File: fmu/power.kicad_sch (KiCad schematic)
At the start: 49 parts, among them IC1 BQ7791500PWT, IC3 BQ25798RQMR, J1 1054500101, Q1 NDT3055L, Q2 NDT3055L, U9 MAX20075ATCA/V+

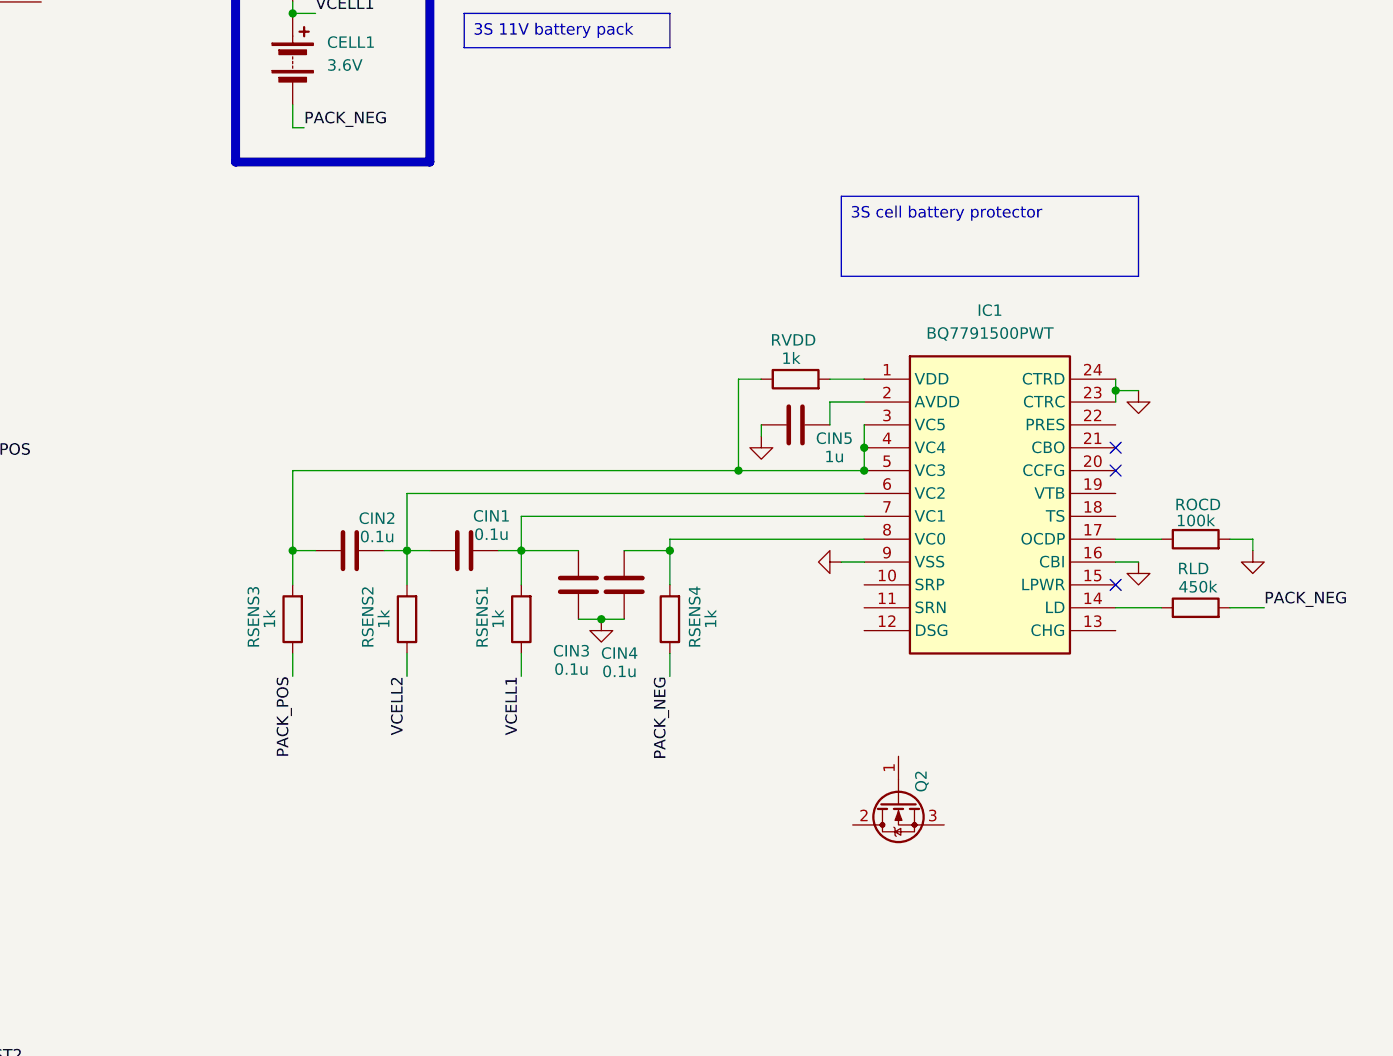
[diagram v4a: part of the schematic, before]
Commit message: BQ7791500 almost completed
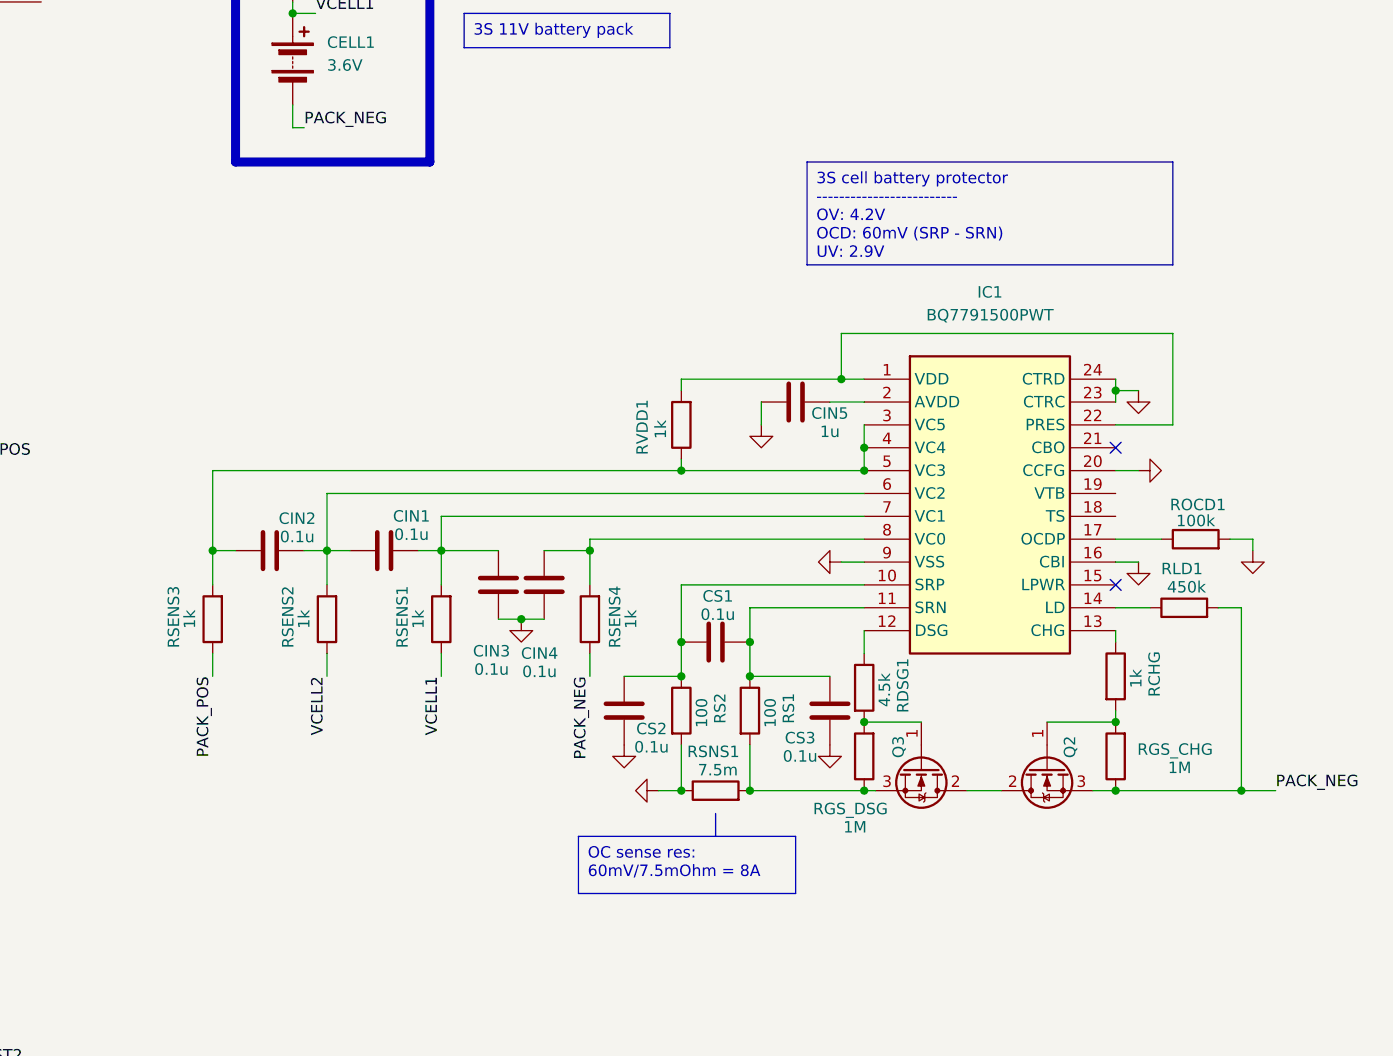
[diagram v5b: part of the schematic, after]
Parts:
- removed RVDD: 1k, Resistor_SMD:R_0603_1608Metric, symbol Device:R
- added CS1, CS2, CS3: 0.1u, Capacitor_SMD:C_0603_1608Metric, symbol Device:C
- added Q3: NDT3055L, Package_TO_SOT_SMD:SOT-223-3_TabPin2, symbol Transistor_FET:NDT3055L
- added RCHG, RVDD1: 1k, Resistor_SMD:R_0603_1608Metric, symbol Device:R
- added RDSG1: 4.5k, Resistor_SMD:R_0603_1608Metric, symbol Device:R
- added RGS_CHG, RGS_DSG: 1M, Resistor_SMD:R_0603_1608Metric, symbol Device:R
- added RS1, RS2: 100, Resistor_SMD:R_0603_1608Metric, symbol Device:R
- added RSNS1: 7.5m, Resistor_SMD:R_0603_1608Metric, symbol Device:R
- renumbered RLD to RLD1, ROCD to ROCD1
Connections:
- net GND: now also IC1.20 (CCFG), CS2.1, CS3.1, RS2.2, RSNS1.1
- net PACK_NEG: now also Q2.3 (S), RGS_CHG.1
- net at IC1.1 (VDD): now also IC1.22 (PRES), RVDD1.2
- net at IC1.10 (SRP): now also CS1.1, CS2.2, RS2.1
- net at IC1.11 (SRN): now also CS1.2, CS3.2, RS1.1
- net at IC1.12 (DSG): now also RDSG1.1
- net at IC1.13 (CHG): now also RCHG.1
- net at CIN2.2, IC1.3 (VC5), IC1.4 (VC4)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: now also RVDD1.1
- net at Q2.1 (G): now also RCHG.2, RGS_CHG.2
- net at Q2.2 (D): now also Q3.2 (D)
- new net: Q3.3 (S), RGS_DSG.1, RS1.2, RSNS1.2
- new net: Q3.1 (G), RDSG1.2, RGS_DSG.2
- no-connect marks 19 -> 18
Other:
- moved on the sheet: CIN1, CIN2, CIN3, CIN4, CIN5, Q2, RLD1, RSENS1, RSENS2, RSENS3, RSENS4

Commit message: Add SD Card reader
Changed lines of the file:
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@@
 		)
 	)
-	(text_box "USB-C 3S battery charger"
+	(text_box "USB-C 3S battery charger\n\n(Set as not mounted due to external charging)"
 		(exclude_from_sim no)
 		(at 54.61 95.25 0)
